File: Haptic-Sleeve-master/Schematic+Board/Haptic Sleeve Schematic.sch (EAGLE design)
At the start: 11 parts, among them CN2 CONNECTOR1, J1 F-1X16-SIP-100-40, M1 MOTORSHORT, M2 MOTORSHORT, M3 MOTORSHORT, M4 MOTORSHORT

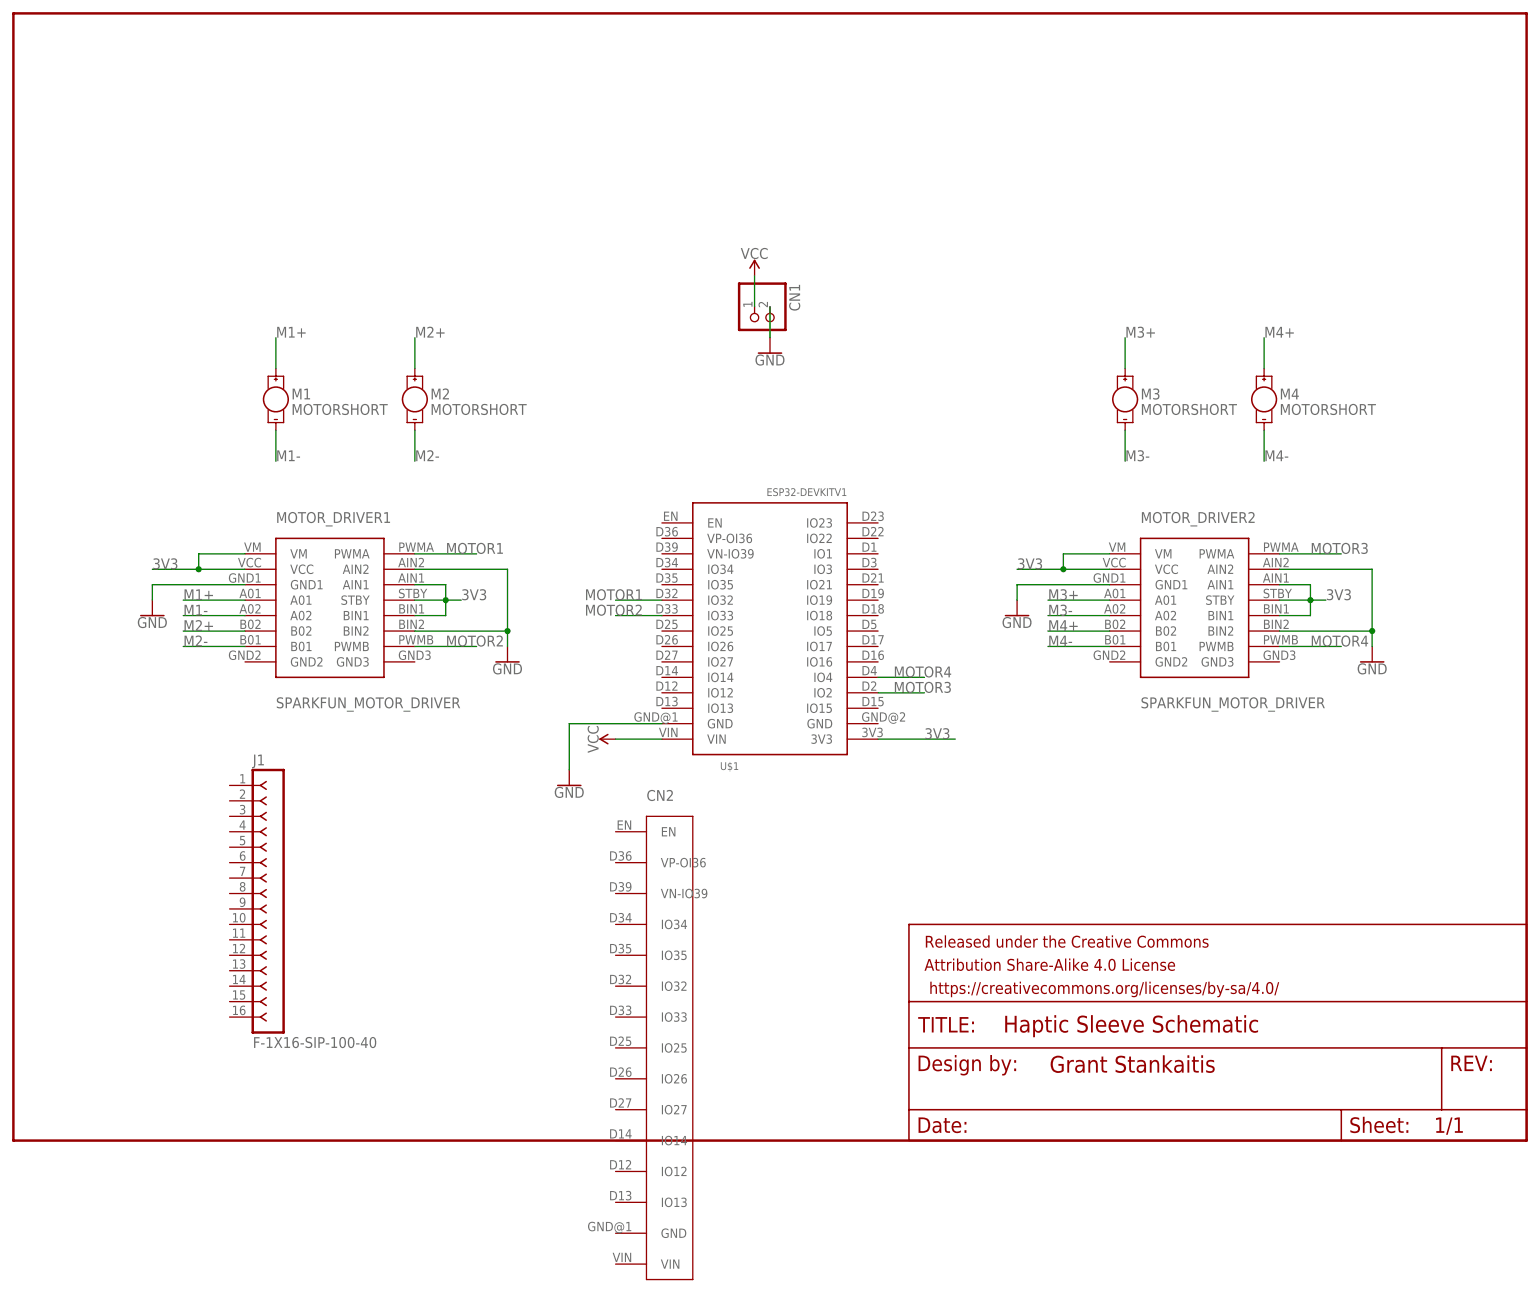
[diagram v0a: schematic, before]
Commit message: adding HapticSleeve3.sch and HapticSleeve3.brd
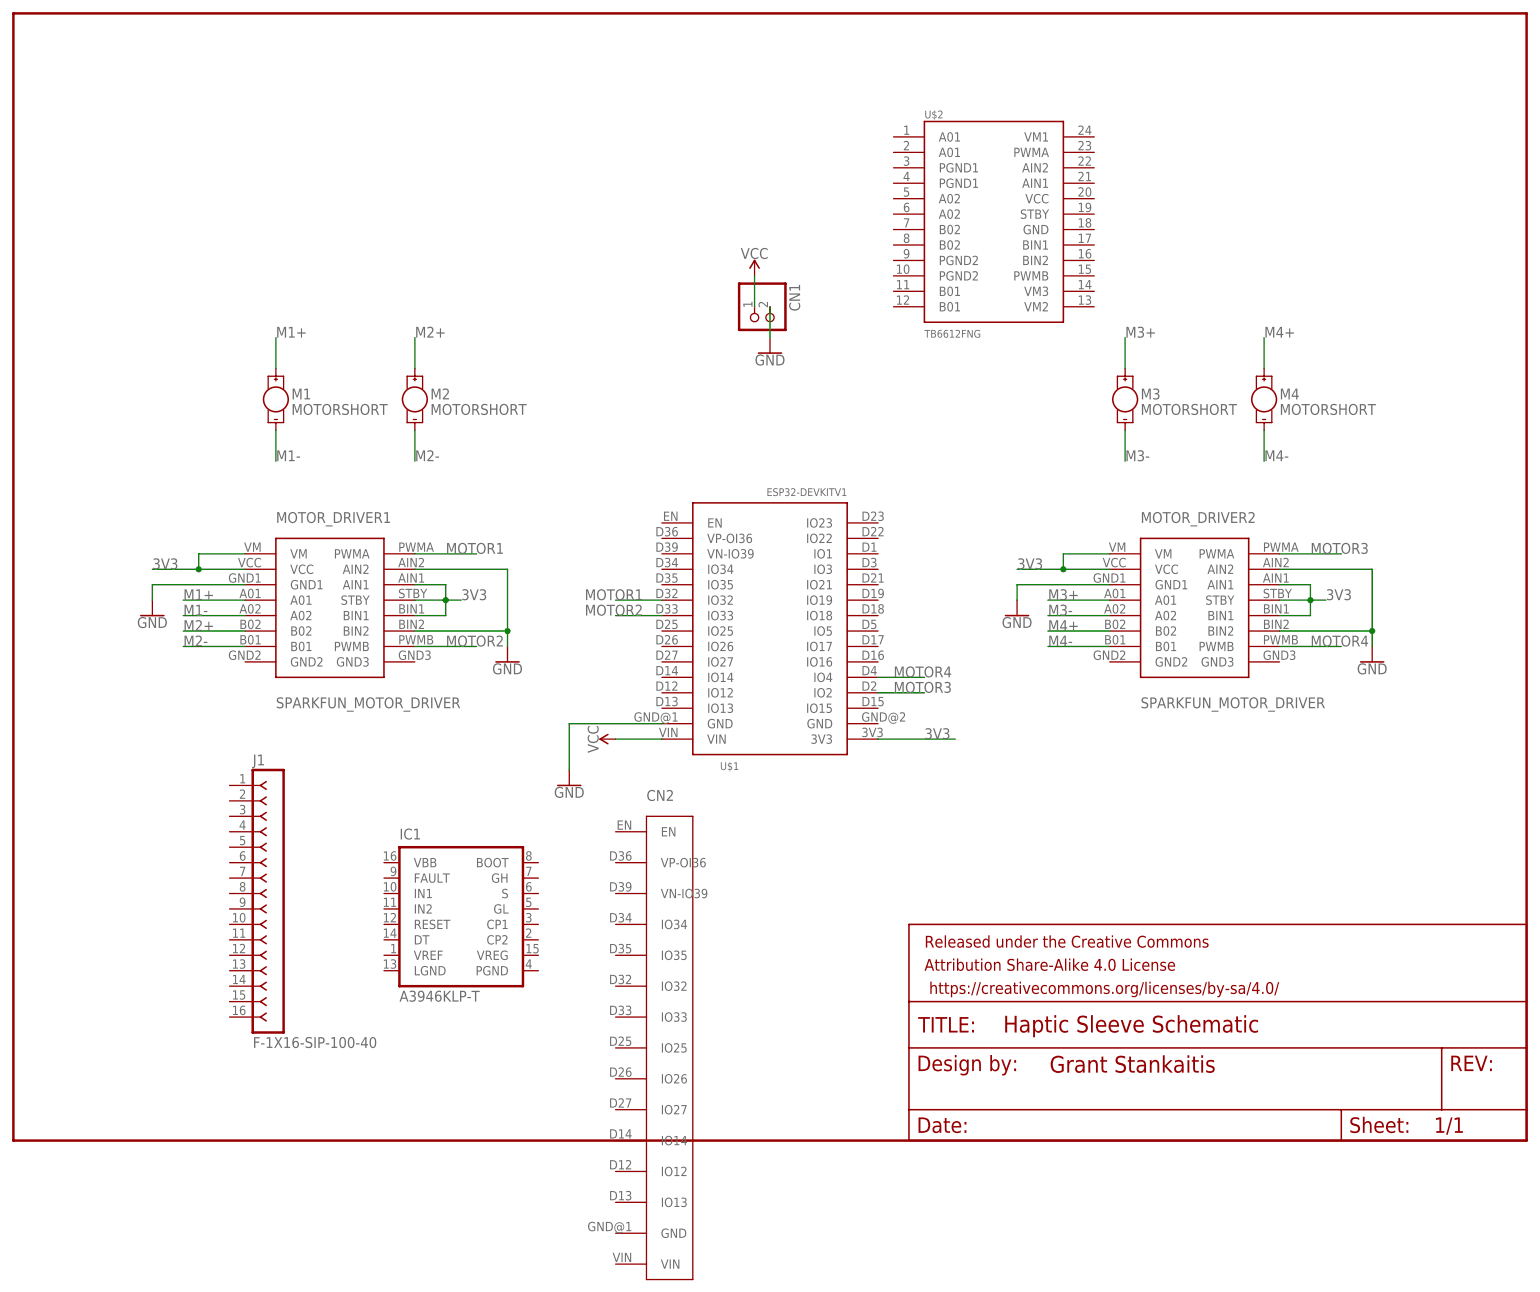
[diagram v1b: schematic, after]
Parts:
- added IC1: A3946KLP-T, allegro:A3946KLP-T
- added U$2: TB6612FNG, SparkFun-IC-Special-Function:TB6612FNG
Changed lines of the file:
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@@
 <part name="J1" library="con-headers-jp-1" deviceset="F-1X16-" device="SIP-100-40"/>
 <part name="CN2" library="1x16connector" deviceset="CONNECTOR1" device=""/>
+<part name="IC1" library="allegro" library_urn="urn:adsk.eagle:library:93" deviceset="A3946" device="" package3d_urn="urn:adsk.eagle:package:3447/1" technology="KLP-T"/>
+<part name="U$2" library="SparkFun-IC-Special-Function" library_urn="urn:adsk.eagle:library:527" deviceset="TB6612FNG" device="" package3d_urn="urn:adsk.eagle:package:39211/1" value="TB6612FNG"/>
 </parts>
 <sheets>
@@
 <instance part="CN2" gate="G$1" x="99.06" y="50.8" smashed="yes">
 <attribute name="NAME" x="104.14" y="55.88" size="1.778" layer="95"/>
+</instance>
+<instance part="IC1" gate="G$1" x="73.66" y="38.1" smashed="yes">
+<attribute name="NAME" x="63.5" y="49.53" size="1.778" layer="95"/>
+<attribute name="VALUE" x="63.5" y="22.86" size="1.778" layer="96"/>
+</instance>
+<instance part="U$2" gate="G$1" x="162.56" y="152.4" smashed="yes">
+<attribute name="NAME" x="149.86" y="168.148" size="1.27" layer="95"/>
+<attribute name="VALUE" x="149.86" y="132.08" size="1.27" layer="96"/>
 </instance>
 </instances>
@@
 </schematic>
 </drawing>
+<compatibility>
+<note version="8.2" severity="warning">
+Since Version 8.2, EAGLE supports online libraries. The ids
+of those online libraries will not be understood (or retained)
+with this version.
+</note>
+<note version="8.3" severity="warning">
+Since Version 8.3, EAGLE supports URNs for individual library
+assets (packages, symbols, and devices). The URNs of those assets
+will not be understood (or retained) with this version.
+</note>
+<note version="8.3" severity="warning">
+Since Version 8.3, EAGLE supports the association of 3D packages
+with devices in libraries, schematics, and board files. Those 3D
+packages will not be understood (or retained) with this version.
+</note>
+</compatibility>
 </eagle>
